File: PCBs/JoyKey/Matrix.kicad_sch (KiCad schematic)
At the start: 24 parts, among them J5 Top Trigger 1, J6 Top Trigger 2, SW2 SW_Push_45deg, SW3 SW_Push_45deg, SW4 SW_Push_45deg, SW5 SW_Push_45deg, SW6 SW_Push_45deg, SW7 SW_Push_45deg

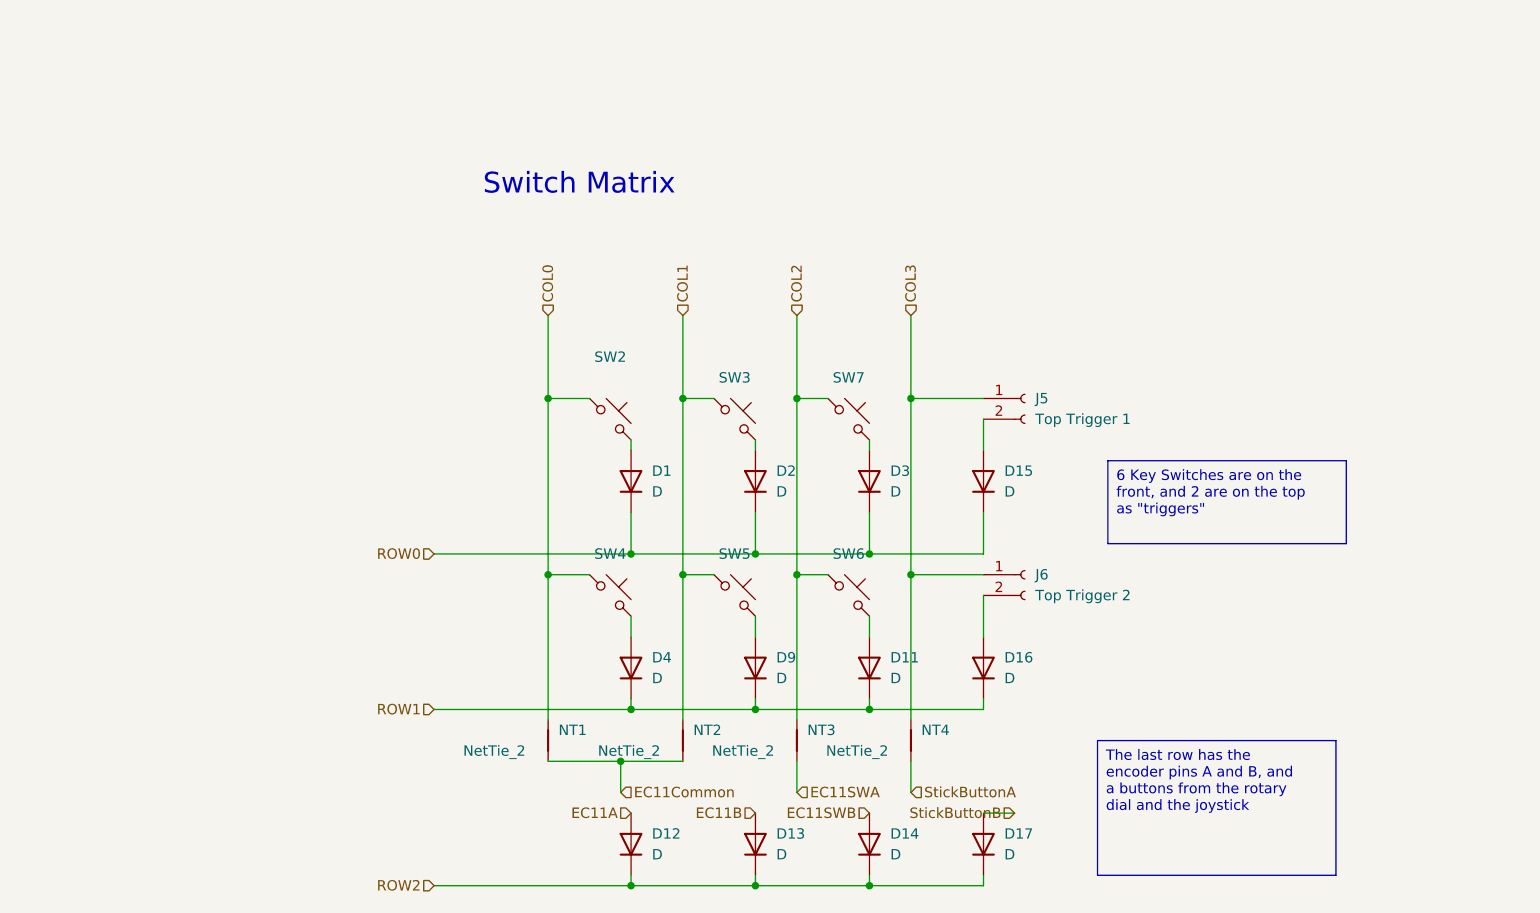
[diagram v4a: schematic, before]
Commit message: Updated Diode to SMD
I don't want through holes because they take up too much space
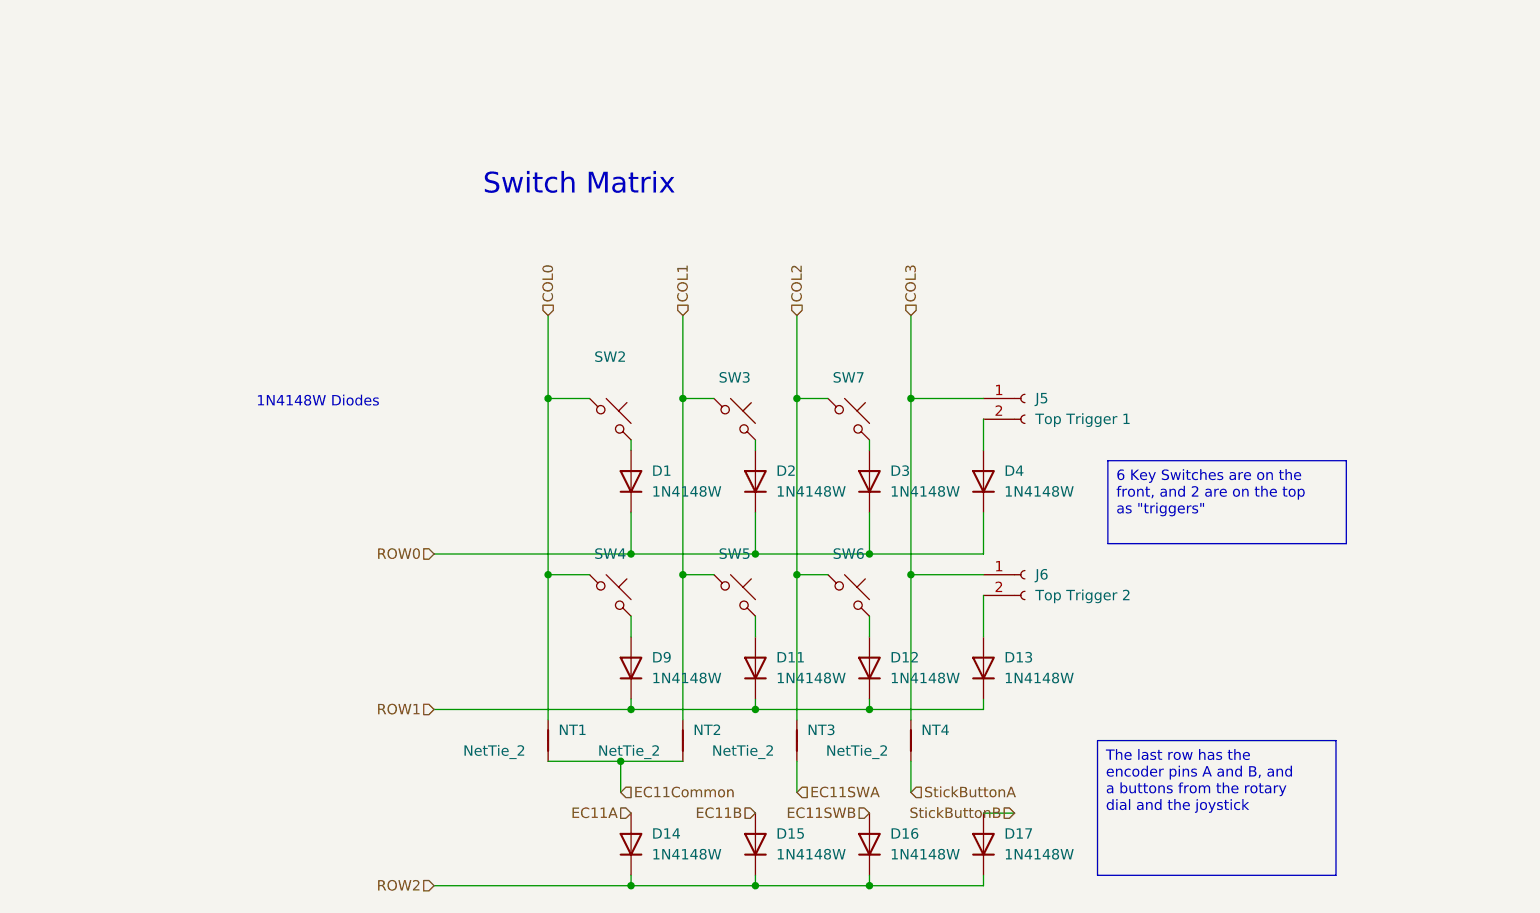
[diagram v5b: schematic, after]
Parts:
- D1, D11, D12, D13, D14, D15, D16, D17, D2, D3, D4, D9: value D -> 1N4148W; footprint Diode_THT:D_DO-35_SOD27_P7.62mm_Horizontal -> Diode_SMD:Nexperia_CFP3_SOD-123W
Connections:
- net EC11A: now also D14.2 (A); no longer D12.2 (A)
- net EC11B: now also D15.2 (A); no longer D13.2 (A)
- net EC11SWB: now also D16.2 (A); no longer D14.2 (A)
- net ROW0: now also D4.1 (K); no longer D15.1 (K)
- net ROW1: now also D12.1 (K), D13.1 (K); no longer D16.1 (K), D4.1 (K)
- net ROW2: now also D15.1 (K), D16.1 (K); no longer D12.1 (K), D13.1 (K)
- net at J6.2 (Pin_2): now also D13.2 (A); no longer D16.2 (A)
- net at SW4.2: now also D9.2 (A); no longer D4.2 (A)
- net at SW5.2: now also D11.2 (A); no longer D9.2 (A)
- net at SW6.2: now also D12.2 (A); no longer D11.2 (A)
- net at J5.2 (Pin_2): now also D4.2 (A); no longer D15.2 (A)
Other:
- note added: "1N4148W Diodes"

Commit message: Re-arranged matrix to have L-shaped clusters
Based on my horizontal layout I really have a 6*2 matrix, however the most switches for the least pins is actually a 4*3. So, I have to great creative with my routing to make it fit.
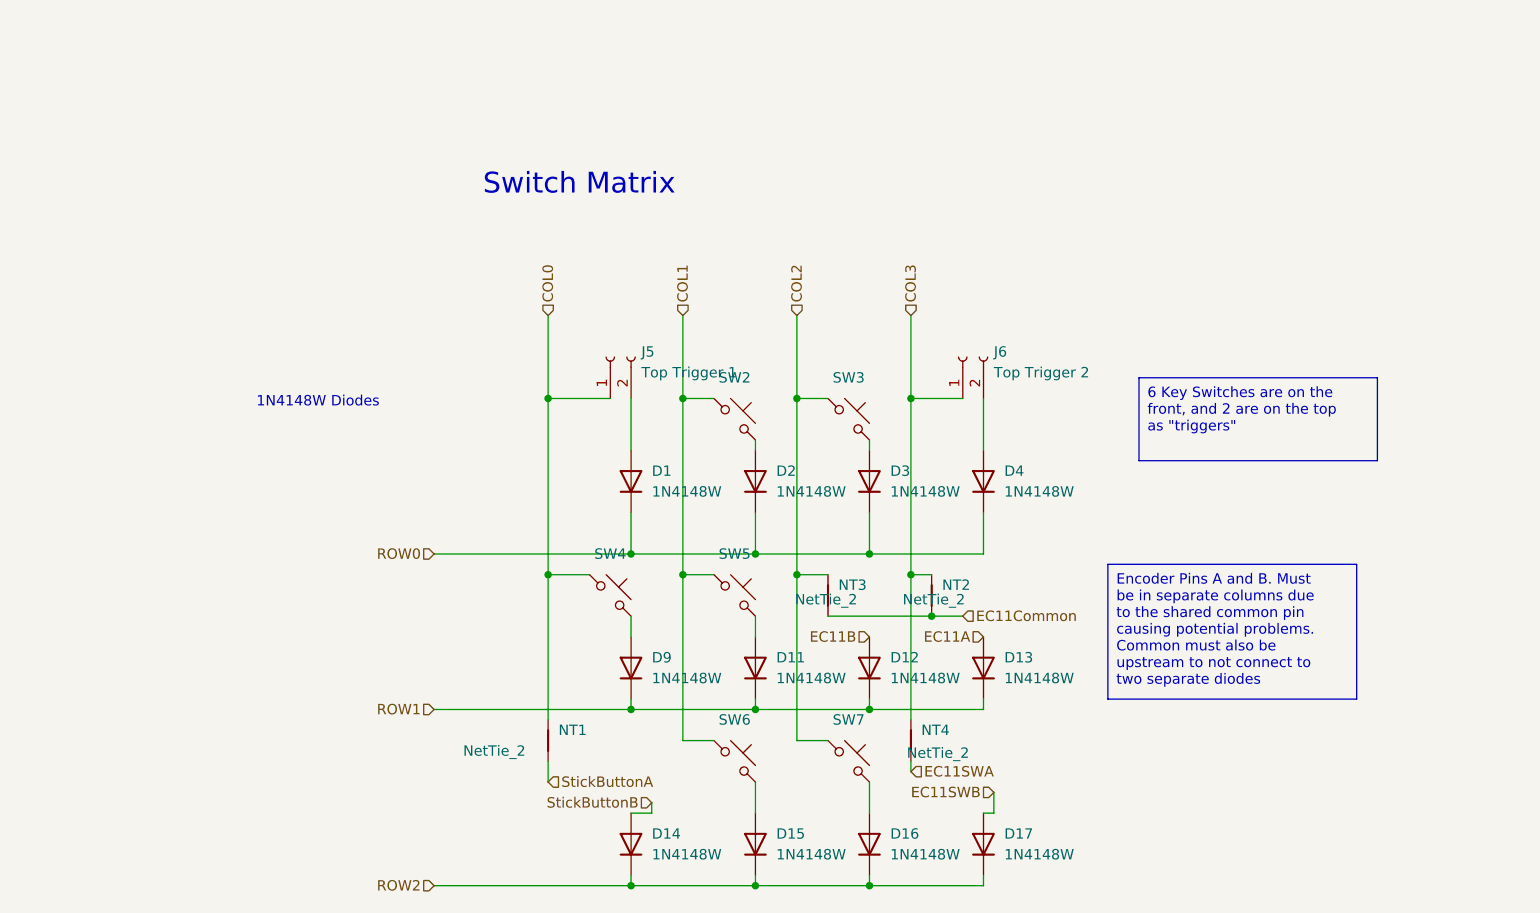
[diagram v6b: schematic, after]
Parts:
- removed SW2: SW_Push_45deg, MX_Solderable:MX-Solderable-1U, symbol Switch:SW_Push_45deg
- added SW3: SW_Push_45deg, MX_Solderable:MX-Solderable-1U, symbol Switch:SW_Push_45deg
- renumbered SW3 to SW2
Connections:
- net COL0: now also J5.1 (Pin_1)
- net COL1: now also SW6.1; no longer NT2.2
- net COL2: now also SW3.1; no longer SW6.1
- net COL3: now also NT2.2; no longer J5.1 (Pin_1)
- net EC11A: now also D13.2 (A); no longer D14.2 (A)
- net EC11B: now also D12.2 (A); no longer D15.2 (A)
- net EC11Common: now also NT3.1; no longer NT1.1
- net EC11SWA: now also NT4.1; no longer NT3.1
- net EC11SWB: now also D17.2 (A); no longer D16.2 (A)
- net StickButtonA: now also NT1.1; no longer NT4.1
- net StickButtonB: now also D14.2 (A); no longer D17.2 (A)
- net at D1.2 (A): now also J5.2 (Pin_2)
- net at J6.2 (Pin_2): now also D4.2 (A); no longer D13.2 (A)
- net at D3.2 (A): now also SW3.2; no longer SW7.2
- net at SW6.2: now also D15.2 (A); no longer D12.2 (A)
- new net: D16.2 (A), SW7.2
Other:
- moved on the sheet: J5, J6, NT2, NT3, SW7

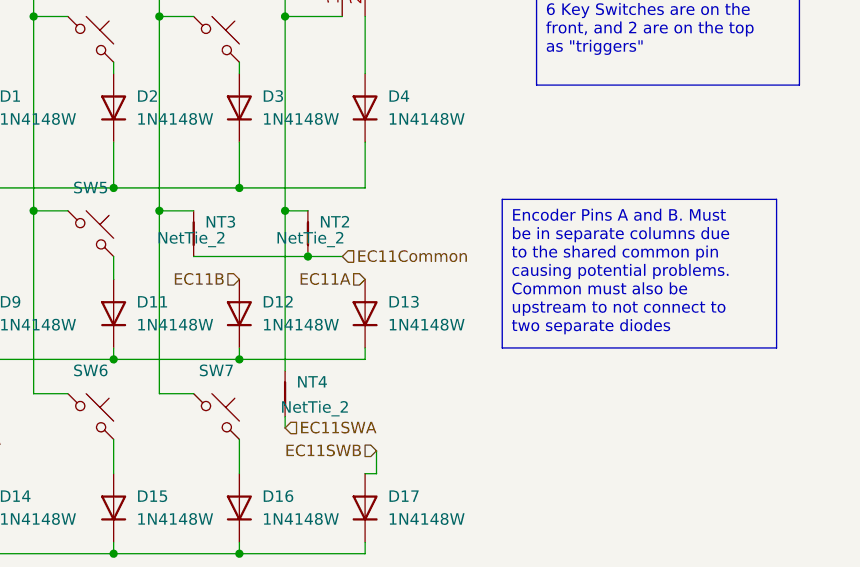
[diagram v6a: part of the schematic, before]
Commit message: Fixed Encoder on Matrix (again)
I got it messed up, A and B should have separate power sources (columns) and common should go to the row. If I had vertical orientation I would have common be on the column and A and B on separate rows. Previous caused a short between columns that could cause ghosting.
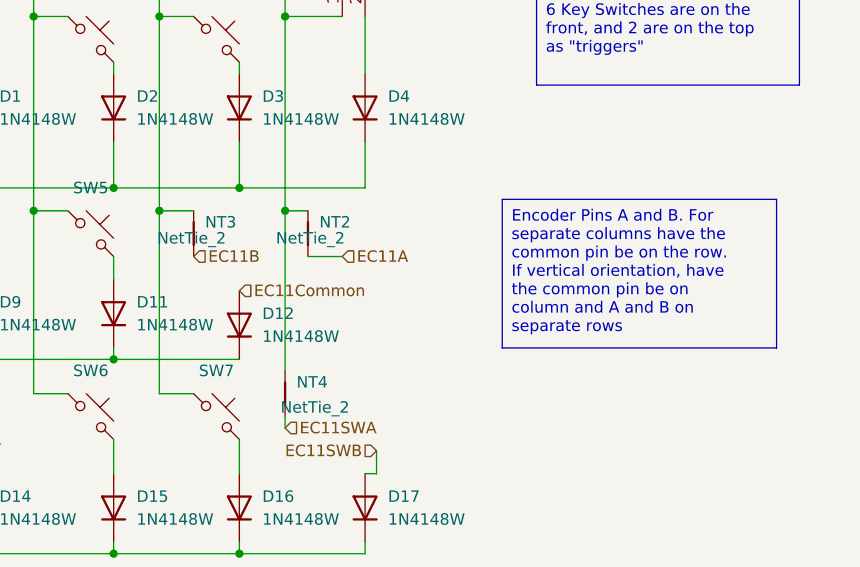
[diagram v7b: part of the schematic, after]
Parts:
- removed D13: 1N4148W, Diode_SMD:Nexperia_CFP3_SOD-123W, symbol Device:D
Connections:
- net EC11A: now also NT2.1
- net EC11B: now also NT3.1; no longer D12.2 (A)
- net EC11Common: now also D12.2 (A); no longer NT2.1, NT3.1
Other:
- moved on the sheet: D12
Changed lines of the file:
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@@
-	)
-	(junction
-		(at 157.48 91.44)
-		(diameter 0)
-		(color 0 0 0 0)
 	)
 	(junction
@@
 	)
 	(junction
-		(at 149.86 102.87)
-		(diameter 0)
-		(color 0 0 0 0)
-	)
-	(junction
 		(at 110.49 86.36)
 		(diameter 0)
@@
 	(wire
 		(pts
-			(xy 149.86 101.6) (xy 149.86 102.87)
-		)
-		(stroke
-			(width 0)
-			(type default)
-		)
-	)
-	(wire
-		(pts
 			(xy 110.49 64.77) (xy 110.49 86.36)
 		)
@@
 	(wire
 		(pts
-			(xy 163.83 101.6) (xy 163.83 102.87)
-		)
-		(stroke
-			(width 0)
-			(type default)
-		)
-	)
-	(wire
-		(pts
 			(xy 135.89 91.44) (xy 135.89 93.98)
 		)
@@
 	(wire
 		(pts
-			(xy 144.78 91.44) (xy 157.48 91.44)
-		)
-		(stroke
-			(width 0)
-			(type default)
-		)
-	)
-	(wire
-		(pts
 			(xy 154.94 64.77) (xy 154.94 86.36)
 		)
@@
 	(wire
 		(pts
-			(xy 149.86 102.87) (xy 163.83 102.87)
-		)
-		(stroke
-			(width 0)
-			(type default)
-		)
-	)
-	(wire
-		(pts
 			(xy 135.89 69.85) (xy 135.89 71.12)
 		)
@@
 		)
 	)
-	(text_box "Encoder Pins A and B. Must be in separate columns due to the shared common pin causing potential problems. Common must also be upstream to not connect to two separate diodes"
+	(text_box "Encoder Pins A and B. For separate columns have the common pin be on the row. If vertical orientation, have the common pin be on column and A and B on separate rows"
 		(exclude_from_sim no)
 		(at 179.07 85.09 0)
@@
 	(hierarchical_label "EC11A"
 		(shape input)
-		(at 163.83 93.98 180)
+		(at 161.29 91.44 0)
 		(effects
 			(font
 				(size 1.27 1.27)
 			)
-			(justify right)
+			(justify left)
 		)
 	)
@@
 	(hierarchical_label "EC11B"
 		(shape input)
-		(at 149.86 93.98 180)
+		(at 144.78 91.44 0)
 		(effects
 			(font
 				(size 1.27 1.27)
 			)
-			(justify right)
+			(justify left)
 		)
 	)
@@
 	(hierarchical_label "EC11Common"
 		(shape input)
-		(at 161.29 91.44 0)
+		(at 149.86 95.25 0)
 		(effects
 			(font
@@
 	(symbol
 		(lib_id "Device:D")
-		(at 149.86 97.79 90)
+		(at 149.86 99.06 90)
 		(unit 1)
 		(exclude_from_sim no)
@@
 		(fields_autoplaced yes)
 		(property "Reference" "D12"
-			(at 152.4 96.5199 90)
+			(at 152.4 97.7899 90)
 			(effects
 				(font
@@
 		)
 		(property "Value" "1N4148W"
-			(at 152.4 99.0599 90)
+			(at 152.4 100.3299 90)
 			(effects
 				(font
@@
 		)
 		(property "Footprint" "Diode_SMD:Nexperia_CFP3_SOD-123W"
-			(at 149.86 97.79 0)
+			(at 149.86 99.06 0)
 			(effects
 				(font
@@
 		)
 		(property "Datasheet" "~"
-			(at 149.86 97.79 0)
+			(at 149.86 99.06 0)
 			(effects
 				(font
@@
 		)
 		(property "Description" "Diode"
-			(at 149.86 97.79 0)
+			(at 149.86 99.06 0)
 			(effects
 				(font
@@
 		)
 		(property "Sim.Device" "D"
-			(at 149.86 97.79 0)
+			(at 149.86 99.06 0)
 			(effects
 				(font
@@
 		)
 		(property "Sim.Pins" "1=K 2=A"
-			(at 149.86 97.79 0)
+			(at 149.86 99.06 0)
 			(effects
 				(font
@@
 					(unit 1)
 				)
-			)
-		)
-	)
-	(symbol
-		(lib_id "Device:D")
-		(at 163.83 97.79 90)
-		(unit 1)
-		(exclude_from_sim no)
-		(in_bom yes)
-		(on_board yes)
-		(dnp no)
-		(fields_autoplaced yes)
-		(property "Reference" "D13"
-			(at 166.37 96.5199 90)
-			(effects
-				(font
-					(size 1.27 1.27)
-				)
-				(justify right)
-			)
-		)
-		(property "Value" "1N4148W"
-			(at 166.37 99.0599 90)
-			(effects
-				(font
-					(size 1.27 1.27)
-				)
-				(justify right)
-			)
-		)
-		(property "Footprint" "Diode_SMD:Nexperia_CFP3_SOD-123W"
-			(at 163.83 97.79 0)
-			(effects
-				(font
-					(size 1.27 1.27)
-				)
-				(hide yes)
-			)
-		)
-		(property "Datasheet" "~"
-			(at 163.83 97.79 0)
-			(effects
-				(font
-					(size 1.27 1.27)
-				)
-				(hide yes)
-			)
-		)
-		(property "Description" "Diode"
-			(at 163.83 97.79 0)
-			(effects
-				(font
-					(size 1.27 1.27)
-				)
-				(hide yes)
-			)
-		)
-		(property "Sim.Device" "D"
-			(at 163.83 97.79 0)
-			(effects
-				(font
-					(size 1.27 1.27)
-				)
-				(hide yes)
-			)
-		)
-		(property "Sim.Pins" "1=K 2=A"
-			(at 163.83 97.79 0)
-			(effects
-				(font
-					(size 1.27 1.27)
-				)
-				(hide yes)
-			)
-		)
-		(pin "1"
-		)
-		(pin "2"
-		)
-		(instances
-			(project "JoyKey"
-				(path "/7995ec7a-c14b-437e-b354-3eb74052b7cb/68ef131f-9d28-47fd-9e2d-054e6cdf50c5"
-					(reference "D13")
-					(unit 1)
-				)

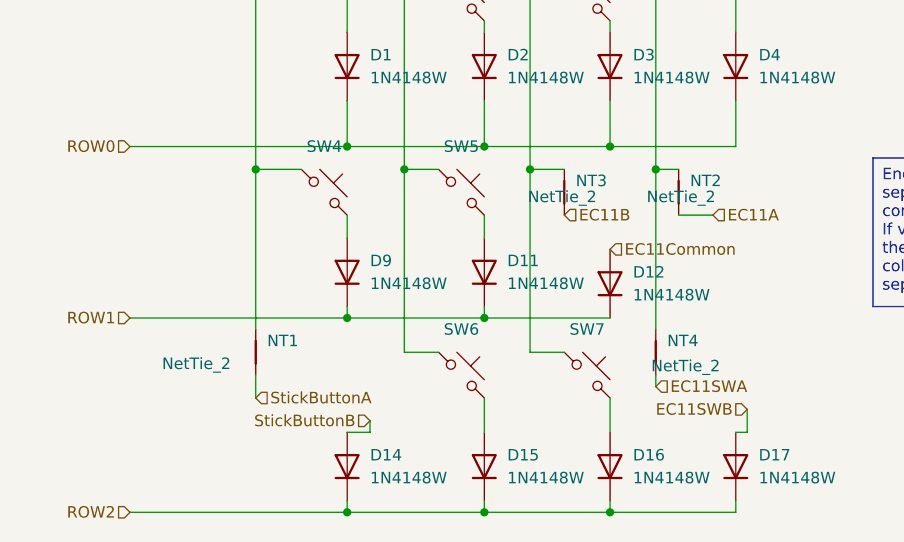
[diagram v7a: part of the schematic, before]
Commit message: Revert "Added netties to matrix for encoder inputs"
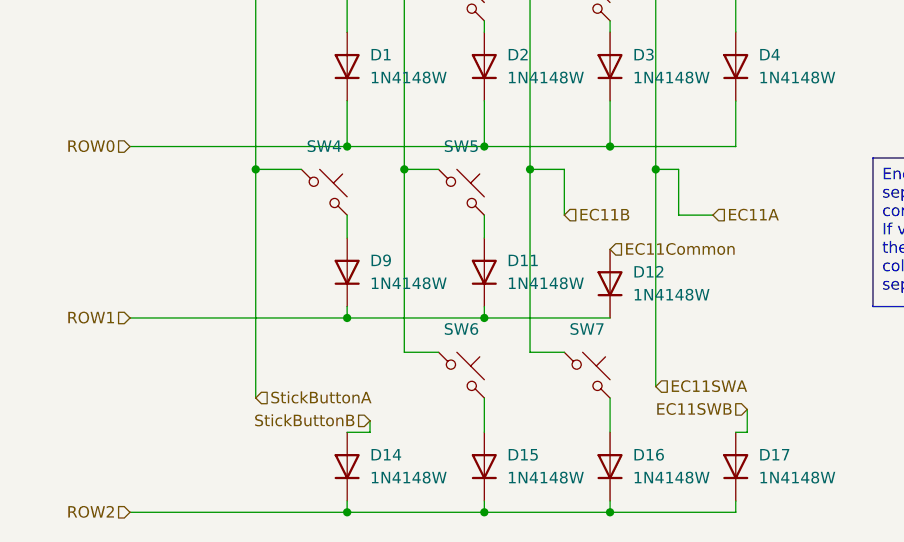
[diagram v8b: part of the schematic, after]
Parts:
- removed NT1, NT2, NT3, NT4: NetTie_2, custom_Connector:NetTie-2_SMD_Pad0.2mm, symbol Device:NetTie_2
